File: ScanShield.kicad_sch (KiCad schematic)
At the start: 20 parts, among them J1 Barrel_Jack_Switch_Pin3Ring, J2 Ringlight, J3 Rotor, J4 Turntable, J5 Cam, J6 Conn_02x20_Odd_Even, J7 Conn_01x15, Q1 IRLZ34N, Q2 IRLZ34N, SW1 SW_SPDT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

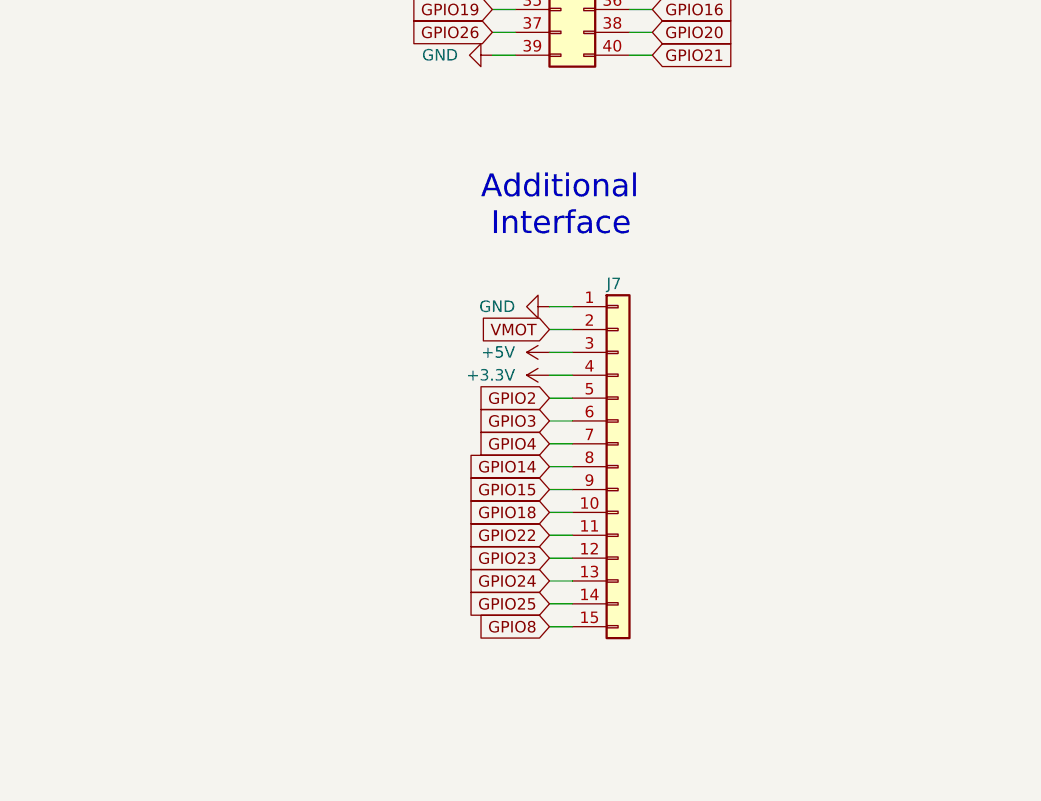
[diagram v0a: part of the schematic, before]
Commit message: Added mounting holes and board outline
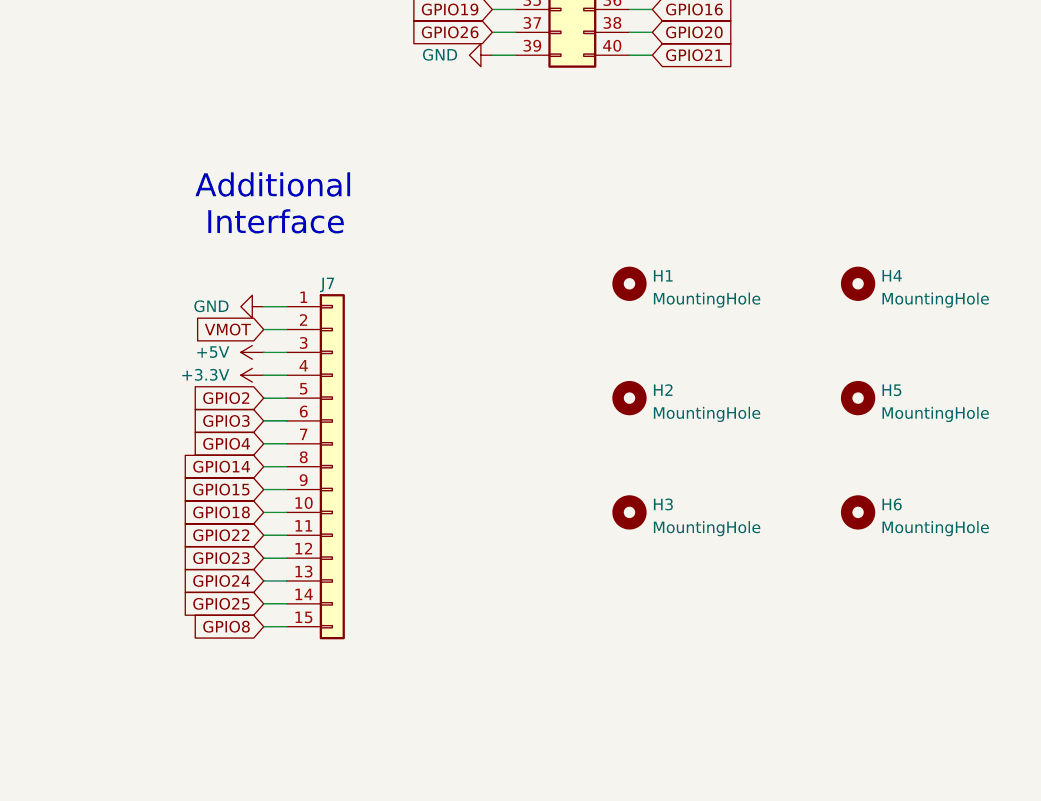
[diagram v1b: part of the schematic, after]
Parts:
- added H1, H2, H3, H4, H5, H6: MountingHole, MountingHole:MountingHole_3.5mm, symbol Mechanical:MountingHole
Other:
- moved on the sheet: J7

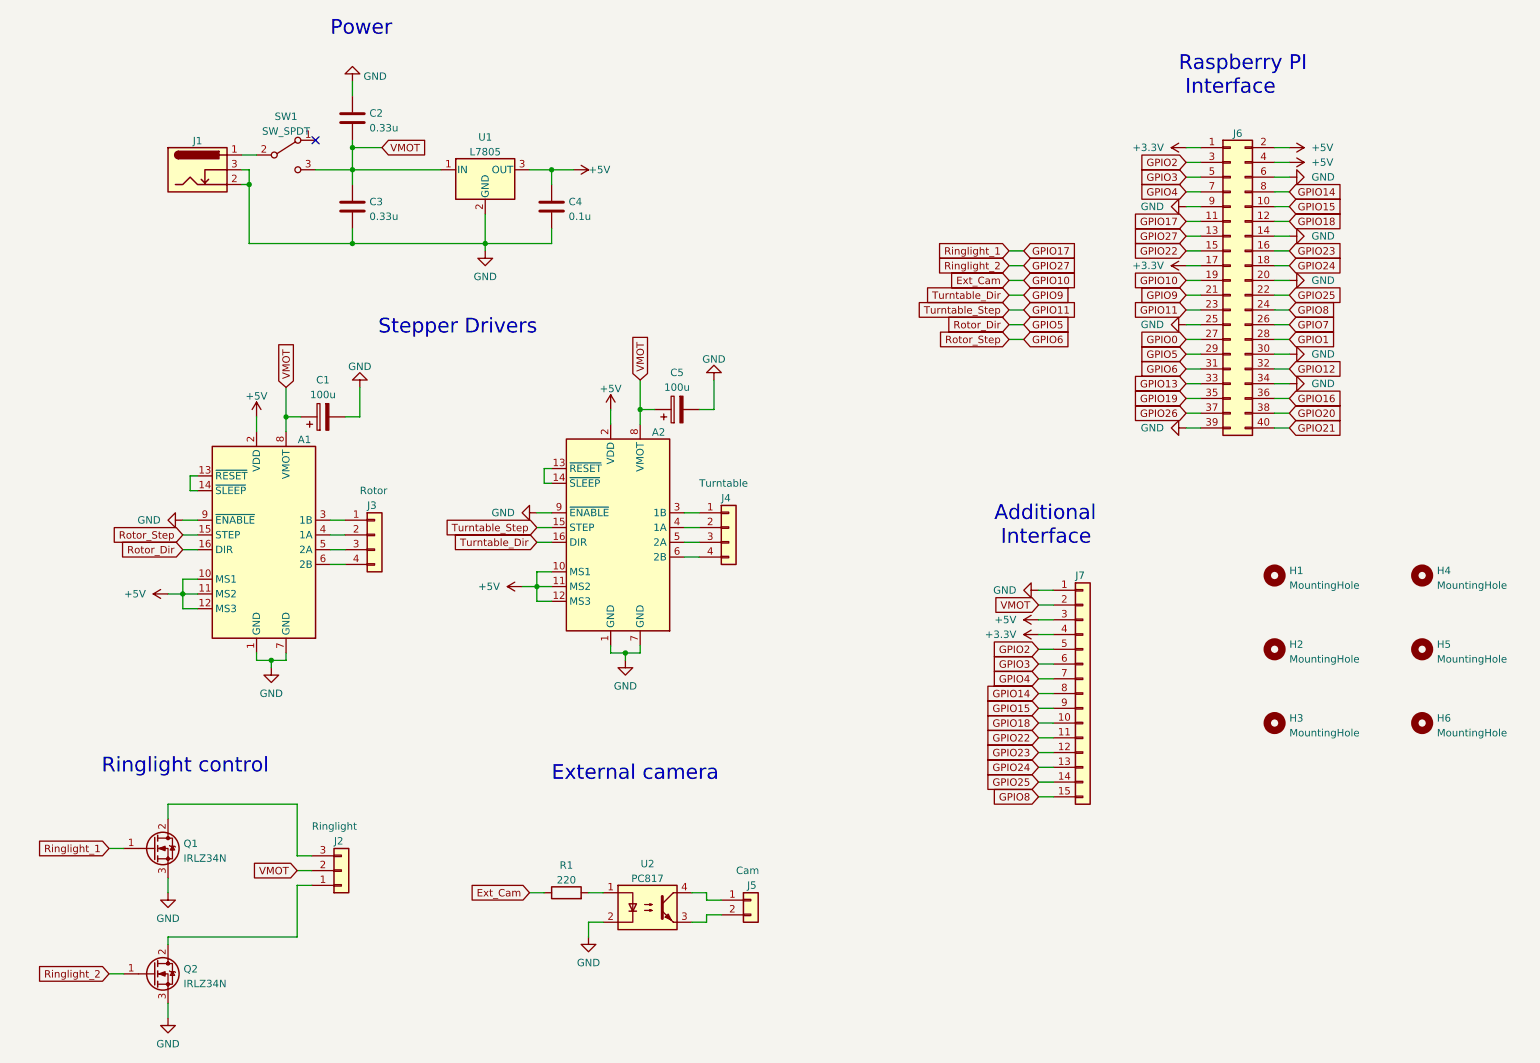
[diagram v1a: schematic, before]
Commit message: Modified pcb, first variant
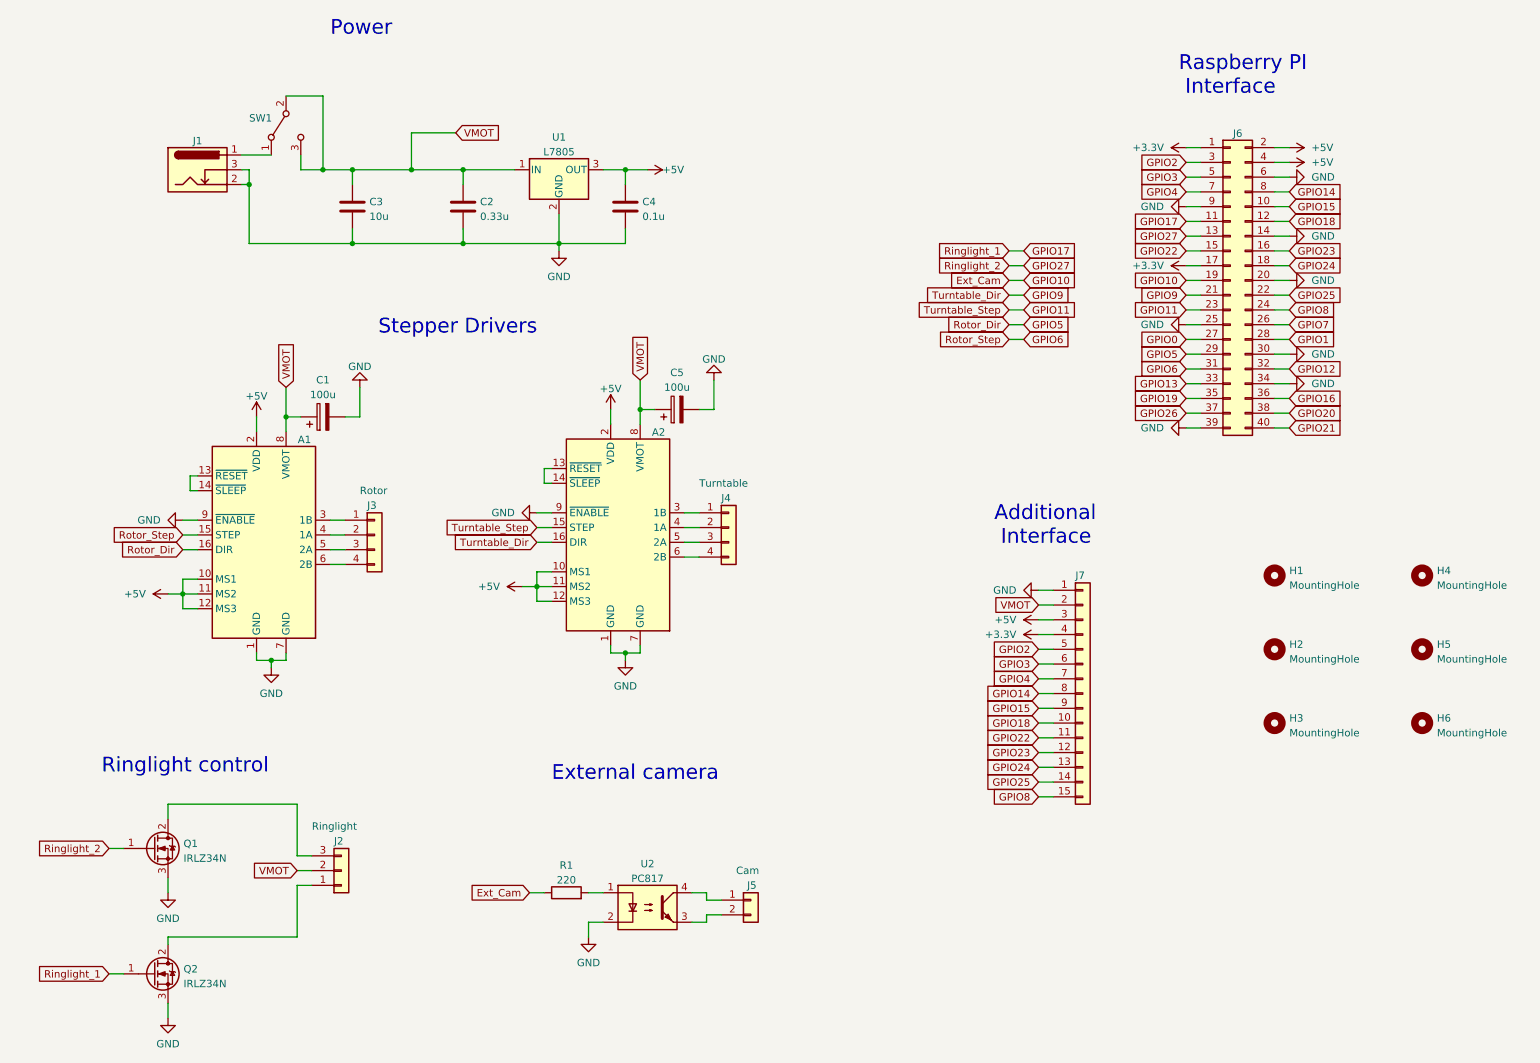
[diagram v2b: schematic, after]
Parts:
- C1, C5: footprint Capacitor_SMD:CP_Elec_6.3x5.4 -> Capacitor_THT:CP_Radial_D6.3mm_P2.50mm
- C3: value 0.33u -> 10u
- J6: footprint Connector_PinHeader_2.54mm:PinHeader_2x20_P2.54mm_Vertical -> Connector_PinSocket_2.54mm:PinSocket_2x20_P2.54mm_Vertical
- Q1, Q2: footprint Package_TO_SOT_THT:TO-220-3_Vertical -> Package_TO_SOT_THT:TO-220-3_Horizontal_TabDown
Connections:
- net GND: now also C2.2; no longer C2.1
- net GPIO17: now also Q2.1 (G); no longer Q1.1 (G)
- net GPIO27: now also Q1.1 (G); no longer Q2.1 (G)
- net VMOT: now also C2.1, SW1.2 (B); no longer C2.2
- net at SW1.1 (A): now also J1.1
- no-connect marks 1 -> 0
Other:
- moved on the sheet: C2, C4, SW1, U1

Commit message: Second pcb draft
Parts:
- removed C2: 0.33u, Capacitor_SMD:C_0805_2012Metric_Pad1.18x1.45mm_HandSolder, symbol Device:C
- Q1, Q2: footprint Package_TO_SOT_THT:TO-220-3_Horizontal_TabDown -> Package_TO_SOT_THT:TO-220-3_Vertical
- U1: footprint Package_TO_SOT_THT:TO-220-3_Horizontal_TabDown -> Connector_PinHeader_2.54mm:PinHeader_1x03_P2.54mm_Vertical
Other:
- moved on the sheet: C4, U1
